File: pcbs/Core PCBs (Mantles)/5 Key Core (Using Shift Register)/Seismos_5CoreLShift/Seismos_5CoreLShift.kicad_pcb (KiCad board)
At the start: 2 copper layers, 147 x 78 mm, 32 parts, among them IC1 74HC595, J1 SM010B-SRSS-TB(LF)(SN), J10 SM10B-SRSS-TB_(LF)(SN), J2 SM010B-SRSS-TB(LF)(SN), J3 SM010B-SRSS-TB(LF)(SN), J4 SM010B-SRSS-TB(LF)(SN), J5 SM010B-SRSS-TB(LF)(SN), J6 SM010B-SRSS-TB(LF)(SN), J7 SM10B-SRSS-TB_(LF)(SN), J8 MJ-4PP-9-Lily58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

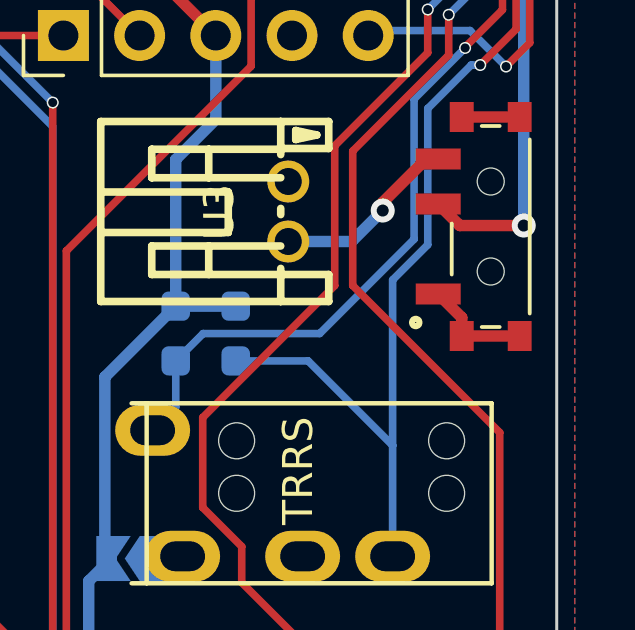
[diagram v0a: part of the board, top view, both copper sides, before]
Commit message: HOTFIX, power switch bridges to ground
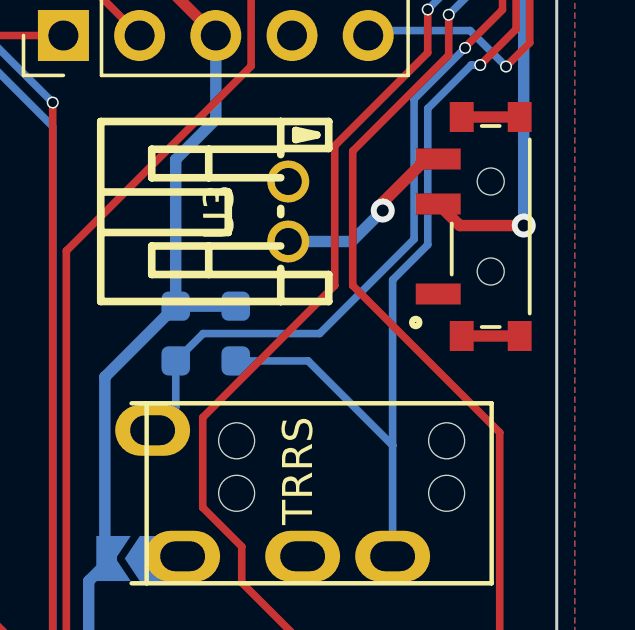
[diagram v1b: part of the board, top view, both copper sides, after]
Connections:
- U2 pad L2: GND -> unconnected-(U2-PadL2)
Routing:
- net GND: track 263.5 -> 261.8 mm

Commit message: Update PCB version and gerbers for HOTFIX
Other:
- board text added: "Rev. 2.1.0"
- board text removed: "Rev. 2.0.0"
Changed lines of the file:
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@@
 		)
 	)
-	(gr_text "Rev. 2.0.0"
+	(gr_text "Rev. 2.1.0"
 		(at 153.55 78.9 270)
 		(layer "B.SilkS")
